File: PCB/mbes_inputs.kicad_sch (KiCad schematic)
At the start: 9 parts

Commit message: feat: power-off button
Because MCU could have a problem for an unpredictable reason, a power-off button has been added to stop the current to the MCU.
But, because I am paranoide and the transistor could have problems, I connected the power-off button yo the MCU too. In this way
it can always shutdown itself
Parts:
- added powerOFF1: Conn_01x02, Connector_PinSocket_2.54mm:PinSocket_1x02_P2.54mm_Vertical, symbol Connector_Generic:Conn_01x02
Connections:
- net GND: now also powerOFF1.1 (Pin_1)
- new net i_powerOFF: powerOFF1.2 (Pin_2)
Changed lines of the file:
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@@
   (junction (at 64.516 135.89) (diameter 0) (color 0 0 0 0)
+  )
+  (junction (at 65.786 157.6324) (diameter 0) (color 0 0 0 0)
   )
   (junction (at 65.786 116.84) (diameter 0) (color 0 0 0 0)
@@
     (stroke (width 0) (type default) (color 0 0 0 0))
   )
+  (wire (pts (xy 95.1992 155.0924) (xy 61.6712 155.0924))
+    (stroke (width 0) (type default) (color 0 0 0 0))
+  )
   (wire (pts (xy 61.722 55.372) (xy 69.977 55.372))
     (stroke (width 0) (type default) (color 0 0 0 0))
@@
     (stroke (width 0) (type default) (color 0 0 0 0))
   )
+  (wire (pts (xy 65.786 157.6324) (xy 65.786 157.6832))
+    (stroke (width 0) (type default) (color 0 0 0 0))
+  )
   (wire (pts (xy 93.472 121.793) (xy 95.504 121.793))
     (stroke (width 0) (type default) (color 0 0 0 0))
@@
     (stroke (width 0) (type default) (color 0 0 0 0))
   )
+  (wire (pts (xy 61.6712 157.6324) (xy 65.786 157.6324))
+    (stroke (width 0) (type default) (color 0 0 0 0))
+  )
   (wire (pts (xy 77.47 44.577) (xy 95.25 44.577))
     (stroke (width 0) (type default) (color 0 0 0 0))
@@
     (stroke (width 0) (type default) (color 0 0 0 0))
   )
+  (wire (pts (xy 65.786 124.968) (xy 65.786 157.6324))
+    (stroke (width 0) (type default) (color 0 0 0 0))
+  )
   (wire (pts (xy 64.516 135.89) (xy 68.326 135.89))
     (stroke (width 0) (type default) (color 0 0 0 0))
@@
     (stroke (width 0) (type default) (color 0 0 0 0))
   )
-  (wire (pts (xy 115.57 124.968) (xy 115.57 155.702))
-    (stroke (width 0) (type default) (color 0 0 0 0))
-  )
   (wire (pts (xy 81.788 148.59) (xy 81.788 138.938))
     (stroke (width 0) (type default) (color 0 0 0 0))
@@
   )
   (wire (pts (xy 61.722 100.584) (xy 65.786 100.584))
-    (stroke (width 0) (type default) (color 0 0 0 0))
-  )
-  (wire (pts (xy 65.786 124.968) (xy 115.57 124.968))
     (stroke (width 0) (type default) (color 0 0 0 0))
   )
@@
     (effects (font (size 1.27 1.27)) (justify left bottom))
   )
+  (global_label "i_powerOFF" (shape input) (at 95.1992 155.0924 0) (fields_autoplaced)
+    (effects (font (size 1.27 1.27)) (justify left))
+    (property "Riferimenti inter-foglio" "${INTERSHEET_REFS}" (id 0) (at 108.1956 155.013 0)
+      (effects (font (size 1.27 1.27)) (justify left) hide)
+    )
+  )
   (global_label "c_engineOFF" (shape input) (at 95.25 51.689 0) (fields_autoplaced)
     (effects (font (size 1.27 1.27)) (justify left))
@@
     (pin "2")
   )
-  (symbol (lib_id "power:GND") (at 115.57 155.702 0) (unit 1)
+  (symbol (lib_id "power:GND") (at 65.786 157.6832 0) (unit 1)
     (in_bom yes) (on_board yes) (fields_autoplaced)
-    (property "Reference" "#PWR0108" (id 0) (at 115.57 162.052 0)
-      (effects (font (size 1.27 1.27)) hide)
-    )
-    (property "Value" "GND" (id 1) (at 115.57 160.782 0))
-    (property "Footprint" "" (id 2) (at 115.57 155.702 0)
-      (effects (font (size 1.27 1.27)) hide)
-    )
-    (property "Datasheet" "" (id 3) (at 115.57 155.702 0)
+    (property "Reference" "#PWR0108" (id 0) (at 65.786 164.0332 0)
+      (effects (font (size 1.27 1.27)) hide)
+    )
+    (property "Value" "GND" (id 1) (at 65.786 162.7632 0))
+    (property "Footprint" "" (id 2) (at 65.786 157.6832 0)
+      (effects (font (size 1.27 1.27)) hide)
+    )
+    (property "Datasheet" "" (id 3) (at 65.786 157.6832 0)
       (effects (font (size 1.27 1.27)) hide)
     )
@@
     (pin "6")
   )
+  (symbol (lib_id "Connector_Generic:Conn_01x02") (at 56.5912 157.6324 180) (unit 1)
+    (in_bom yes) (on_board yes)
+    (property "Reference" "powerOFF1" (id 0) (at 62.4332 151.7904 0)
+      (effects (font (size 1.27 1.27)) (justify left))
+    )
+    (property "Value" "Conn_01x02" (id 1) (at 55.3213 160.1724 90)
+      (effects (font (size 1.27 1.27)) (justify left) hide)
+    )
+    (property "Footprint" "Connector_PinSocket_2.54mm:PinSocket_1x02_P2.54mm_Vertical" (id 2) (at 56.5912 157.6324 0)
+      (effects (font (size 1.27 1.27)) hide)
+    )
+    (property "Datasheet" "~" (id 3) (at 56.5912 157.6324 0)
+      (effects (font (size 1.27 1.27)) hide)
+    )
+    (pin "1")
+    (pin "2")
+  )
 )

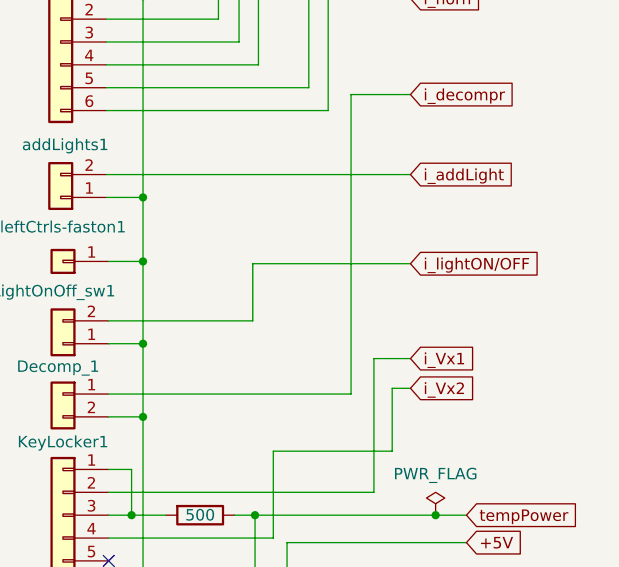
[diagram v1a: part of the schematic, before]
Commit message: - Other floating BC337 transistors bases fixed - USB port missing fixed - Small enhancements
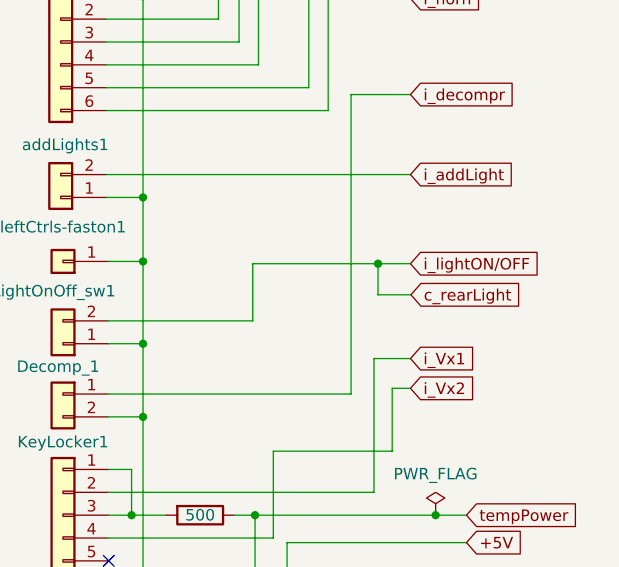
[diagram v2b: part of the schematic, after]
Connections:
- net i_lightON/OFF renamed c_rearLight
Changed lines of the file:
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@@
   (junction (at 78.232 135.89) (diameter 0) (color 0 0 0 0)
+  )
+  (junction (at 91.8972 107.95) (diameter 0) (color 0 0 0 0)
   )
   (junction (at 65.786 107.696) (diameter 0) (color 0 0 0 0)
@@
     (stroke (width 0) (type default) (color 0 0 0 0))
   )
+  (wire (pts (xy 91.8972 107.95) (xy 95.504 107.95))
+    (stroke (width 0) (type default) (color 0 0 0 0))
+  )
   (wire (pts (xy 65.786 107.696) (xy 65.786 100.584))
     (stroke (width 0) (type default) (color 0 0 0 0))
@@
     (stroke (width 0) (type default) (color 0 0 0 0))
   )
+  (wire (pts (xy 95.5548 111.4044) (xy 91.8972 111.4044))
+    (stroke (width 0) (type default) (color 0 0 0 0))
+  )
   (wire (pts (xy 61.722 98.044) (xy 95.504 98.044))
     (stroke (width 0) (type default) (color 0 0 0 0))
@@
     (stroke (width 0) (type default) (color 0 0 0 0))
   )
+  (wire (pts (xy 91.8972 111.4044) (xy 91.8972 107.95))
+    (stroke (width 0) (type default) (color 0 0 0 0))
+  )
   (wire (pts (xy 61.976 135.89) (xy 64.516 135.89))
     (stroke (width 0) (type default) (color 0 0 0 0))
@@
     (stroke (width 0) (type default) (color 0 0 0 0))
   )
-  (wire (pts (xy 77.978 107.95) (xy 95.504 107.95))
+  (wire (pts (xy 77.978 107.95) (xy 91.8972 107.95))
     (stroke (width 0) (type default) (color 0 0 0 0))
   )
@@
       (effects (font (size 1.27 1.27)) (justify left) hide)
     )
+  )
+  (global_label "c_rearLight" (shape input) (at 95.5548 111.4044 0) (fields_autoplaced)
+    (effects (font (size 1.27 1.27)) (justify left))
+    (property "Riferimenti inter-foglio" "${INTERSHEET_REFS}" (id 0) (at 108.4908 111.325 0)
+      (effects (font (size 1.27 1.27)) (justify left) hide)
+    )

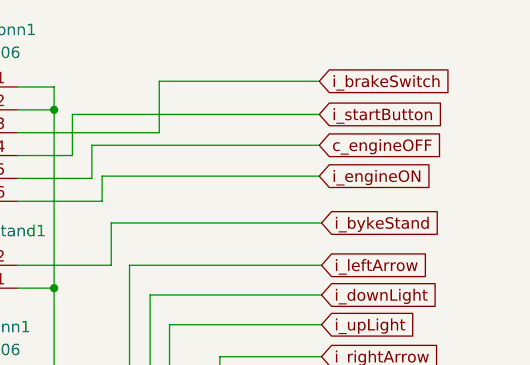
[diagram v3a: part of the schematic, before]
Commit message: Fixes and optimizations (unuseful I/O lines dropped)
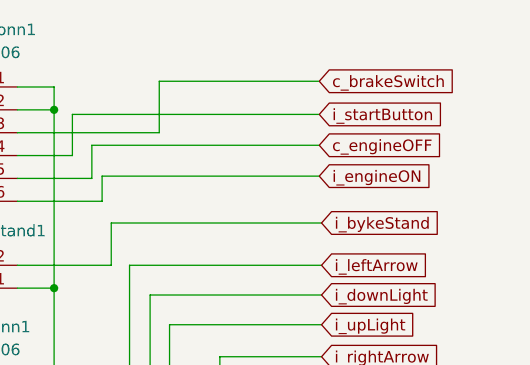
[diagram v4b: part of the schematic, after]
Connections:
- net i_brakeSwitch renamed c_brakeSwitch
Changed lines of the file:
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@@
     )
   )
-  (global_label "i_brakeSwitch" (shape input) (at 95.25 44.577 0) (fields_autoplaced)
+  (global_label "c_brakeSwitch" (shape input) (at 95.25 44.577 0) (fields_autoplaced)
     (effects (font (size 1.27 1.27)) (justify left))
-    (property "Riferimenti inter-foglio" "${INTERSHEET_REFS}" (id 0) (at 110.5445 44.4976 0)
+    (property "Riferimenti inter-foglio" "${INTERSHEET_REFS}" (id 0) (at 111.0283 44.4976 0)
       (effects (font (size 1.27 1.27)) (justify left) hide)
     )

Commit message: fixes...
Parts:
- R1: value 500 -> 1K; footprint Resistor_THT:R_Axial_DIN0309_L9.0mm_D3.2mm_P12.70mm_Horizontal -> Resistor_THT:R_Axial_DIN0207_L6.3mm_D2.5mm_P10.16mm_Horizontal
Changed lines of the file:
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@@
       (effects (font (size 1.27 1.27)) hide)
     )
-    (property "Value" "500" (id 1) (at 72.136 135.89 90))
-    (property "Footprint" "Resistor_THT:R_Axial_DIN0309_L9.0mm_D3.2mm_P12.70mm_Horizontal" (id 2) (at 72.136 134.112 90)
+    (property "Value" "1K" (id 1) (at 72.136 135.89 90))
+    (property "Footprint" "Resistor_THT:R_Axial_DIN0207_L6.3mm_D2.5mm_P10.16mm_Horizontal" (id 2) (at 72.136 134.112 90)
       (effects (font (size 1.27 1.27)) hide)
     )

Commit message: PCB splitted
In order to use the debug support, it has been needed to add the ISP port. But it means to loose 4 pins.
So, I have added a I/O extender chip on I2C bus (other 2 pins lost). Because the complexity has encreased
I have had to split the PCB in thwo different ones.
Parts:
- Bike_stand1, Decomp_1, LightOnOff_sw1, addLights1, powerOFF1: footprint Connector_PinSocket_2.54mm:PinSocket_1x02_P2.54mm_Vertical -> Connector_Wire:SolderWire-0.5sqmm_1x02_P4.6mm_D0.9mm_OD2.1mm
- R1: footprint Resistor_THT:R_Axial_DIN0207_L6.3mm_D2.5mm_P10.16mm_Horizontal -> Resistor_THT:R_Axial_DIN0207_L6.3mm_D2.5mm_P7.62mm_Horizontal
- leftCtrls-faston1: footprint Connector_Wire:SolderWire-0.75sqmm_1x01_D1.25mm_OD2.3mm -> Connector_Wire:SolderWire-0.5sqmm_1x01_D0.9mm_OD2.1mm
- leftCtrls_conn1, rightCtrls_conn1: footprint Connector_PinHeader_2.54mm:PinHeader_1x06_P2.54mm_Vertical -> Connector_Wire:SolderWire-0.5sqmm_1x06_P4.6mm_D0.9mm_OD2.1mm
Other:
- company: (none) -> Panicosoft
- title: (none) -> Motorbike lights and services controller
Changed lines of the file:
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@@
 (kicad_sch (version 20211123) (generator eeschema)
   (paper "A4")
+  (title_block
+    (title "Motorbike lights and services controller")
+    (rev "4.0")
+    (company "Panicosoft")
+    (comment 1 "Logic controller unit")
+    (comment 2 "Motorbiker's buttons and switches controls")
+  )
   (junction (at 64.516 135.89) (diameter 0) (color 0 0 0 0)
   )
@@
       (effects (font (size 1.27 1.27)) hide)
     )
-    (property "Footprint" "Connector_PinSocket_2.54mm:PinSocket_1x02_P2.54mm_Vertical" (id 2) (at 56.642 67.564 0)
+    (property "Footprint" "Connector_Wire:SolderWire-0.5sqmm_1x02_P4.6mm_D0.9mm_OD2.1mm" (id 2) (at 56.642 67.564 0)
       (effects (font (size 1.27 1.27)) hide)
     )
@@
       (effects (font (size 1.27 1.27)) (justify left) hide)
     )
-    (property "Footprint" "Connector_PinSocket_2.54mm:PinSocket_1x02_P2.54mm_Vertical" (id 2) (at 56.896 116.84 0)
+    (property "Footprint" "Connector_Wire:SolderWire-0.5sqmm_1x02_P4.6mm_D0.9mm_OD2.1mm" (id 2) (at 56.896 116.84 0)
       (effects (font (size 1.27 1.27)) hide)
     )
@@
     (property "Reference" "leftCtrls_conn1" (id 0) (at 56.642 71.882 0))
     (property "Value" "Conn_01x06" (id 1) (at 56.642 74.422 0))
-    (property "Footprint" "Connector_PinHeader_2.54mm:PinHeader_1x06_P2.54mm_Vertical" (id 2) (at 56.642 83.312 0)
+    (property "Footprint" "Connector_Wire:SolderWire-0.5sqmm_1x06_P4.6mm_D0.9mm_OD2.1mm" (id 2) (at 56.642 83.312 0)
       (effects (font (size 1.27 1.27)) hide)
     )
@@
       (effects (font (size 1.27 1.27)) (justify left) hide)
     )
-    (property "Footprint" "Connector_PinSocket_2.54mm:PinSocket_1x02_P2.54mm_Vertical" (id 2) (at 56.642 100.584 0)
+    (property "Footprint" "Connector_Wire:SolderWire-0.5sqmm_1x02_P4.6mm_D0.9mm_OD2.1mm" (id 2) (at 56.642 100.584 0)
       (effects (font (size 1.27 1.27)) hide)
     )
@@
       (effects (font (size 1.27 1.27)) hide)
     )
-    (property "Footprint" "Connector_PinSocket_2.54mm:PinSocket_1x02_P2.54mm_Vertical" (id 2) (at 56.896 122.428 0)
+    (property "Footprint" "Connector_Wire:SolderWire-0.5sqmm_1x02_P4.6mm_D0.9mm_OD2.1mm" (id 2) (at 56.896 122.428 0)
       (effects (font (size 1.27 1.27)) hide)
     )
@@
       (effects (font (size 1.27 1.27)) hide)
     )
-    (property "Footprint" "Connector_Wire:SolderWire-0.75sqmm_1x01_D1.25mm_OD2.3mm" (id 2) (at 56.896 107.696 0)
+    (property "Footprint" "Connector_Wire:SolderWire-0.5sqmm_1x01_D0.9mm_OD2.1mm" (id 2) (at 56.896 107.696 0)
       (effects (font (size 1.27 1.27)) hide)
     )
@@
     )
     (property "Value" "1K" (id 1) (at 72.136 135.89 90))
-    (property "Footprint" "Resistor_THT:R_Axial_DIN0207_L6.3mm_D2.5mm_P10.16mm_Horizontal" (id 2) (at 72.136 134.112 90)
+    (property "Footprint" "Resistor_THT:R_Axial_DIN0207_L6.3mm_D2.5mm_P7.62mm_Horizontal" (id 2) (at 72.136 134.112 90)
       (effects (font (size 1.27 1.27)) hide)
     )
@@
     (property "Reference" "rightCtrls_conn1" (id 0) (at 56.642 38.862 0))
     (property "Value" "Conn_01x06" (id 1) (at 56.642 41.402 0))
-    (property "Footprint" "Connector_PinHeader_2.54mm:PinHeader_1x06_P2.54mm_Vertical" (id 2) (at 56.642 50.292 0)
+    (property "Footprint" "Connector_Wire:SolderWire-0.5sqmm_1x06_P4.6mm_D0.9mm_OD2.1mm" (id 2) (at 56.642 50.292 0)
       (effects (font (size 1.27 1.27)) hide)
     )
@@
       (effects (font (size 1.27 1.27)) (justify left) hide)
     )
-    (property "Footprint" "Connector_PinSocket_2.54mm:PinSocket_1x02_P2.54mm_Vertical" (id 2) (at 56.5912 157.6324 0)
-      (effects (font (size 1.27 1.27)) hide)
-    )
+    (property "Footprint" "Connector_Wire:SolderWire-0.5sqmm_1x02_P4.6mm_D0.9mm_OD2.1mm" (id 2) (at 56.5912 157.6324 0)
+      (effects (font (size 1.27 1.27)) hide)
+    )
